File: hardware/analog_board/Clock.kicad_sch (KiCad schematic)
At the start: 13 parts, among them J3 Conn_01x04_Pin, J7 CH1, U8 CDCI6214RGER, Y1 ASE-10MHz

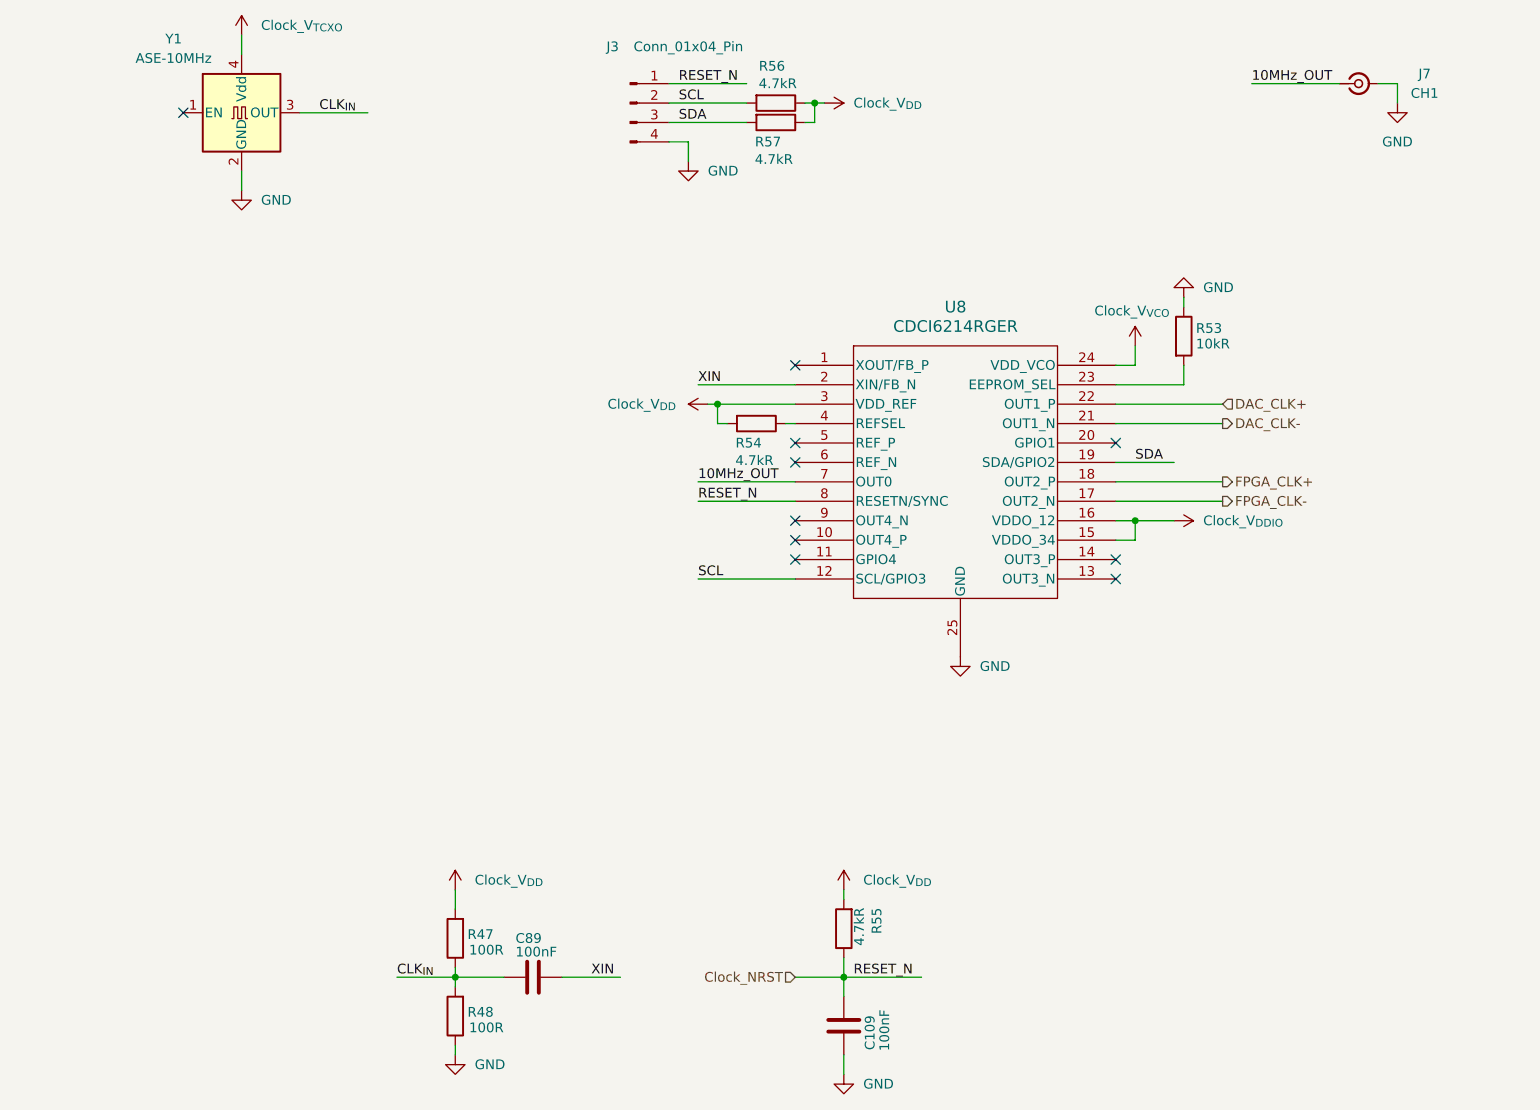
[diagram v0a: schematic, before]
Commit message: debug：修正原理图部分错误
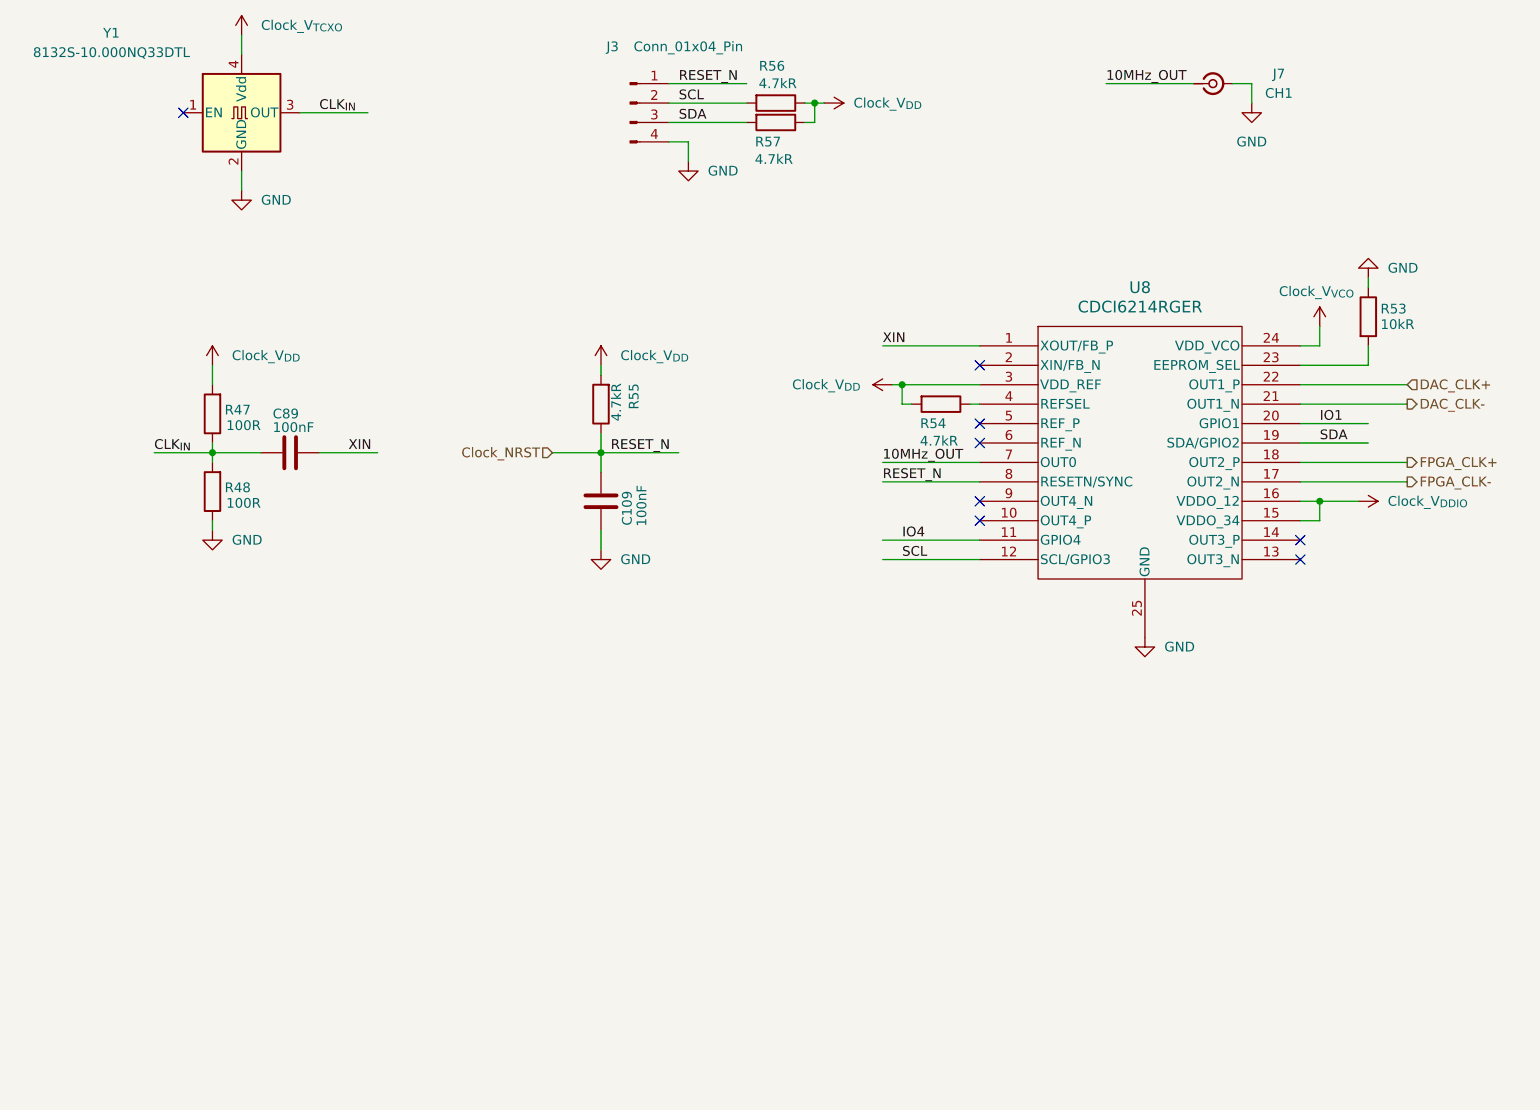
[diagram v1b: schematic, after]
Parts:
- Y1: value ASE-10MHz -> 8132S-10.000NQ33DTL
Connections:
- net XIN: now also U8.1 (XOUT/FB_P); no longer U8.2 (XIN/FB_N)
- net IO4: now reaches U8.11 (GPIO4)
- net IO1: now reaches U8.20 (GPIO1)
- no-connect marks 10 -> 8
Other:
- moved on the sheet: C109, C89, J7, R47, R48, R53, R54, R55, U8

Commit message: feat：BOM导出
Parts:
- J7: value CH1 -> SMA
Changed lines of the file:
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@@
 			)
 		)
-		(property "Value" "CH1"
+		(property "Value" "SMA"
 			(at 183.896 54.61 0)
 			(show_name no)
